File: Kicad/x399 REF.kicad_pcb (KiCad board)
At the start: 2 copper layers, 106 x 56 mm, 57 parts, among them J1 +15V, J2 10Vref, Q1 MMBT3904, Q2 2SD882, U1 LM399, U2 OP07

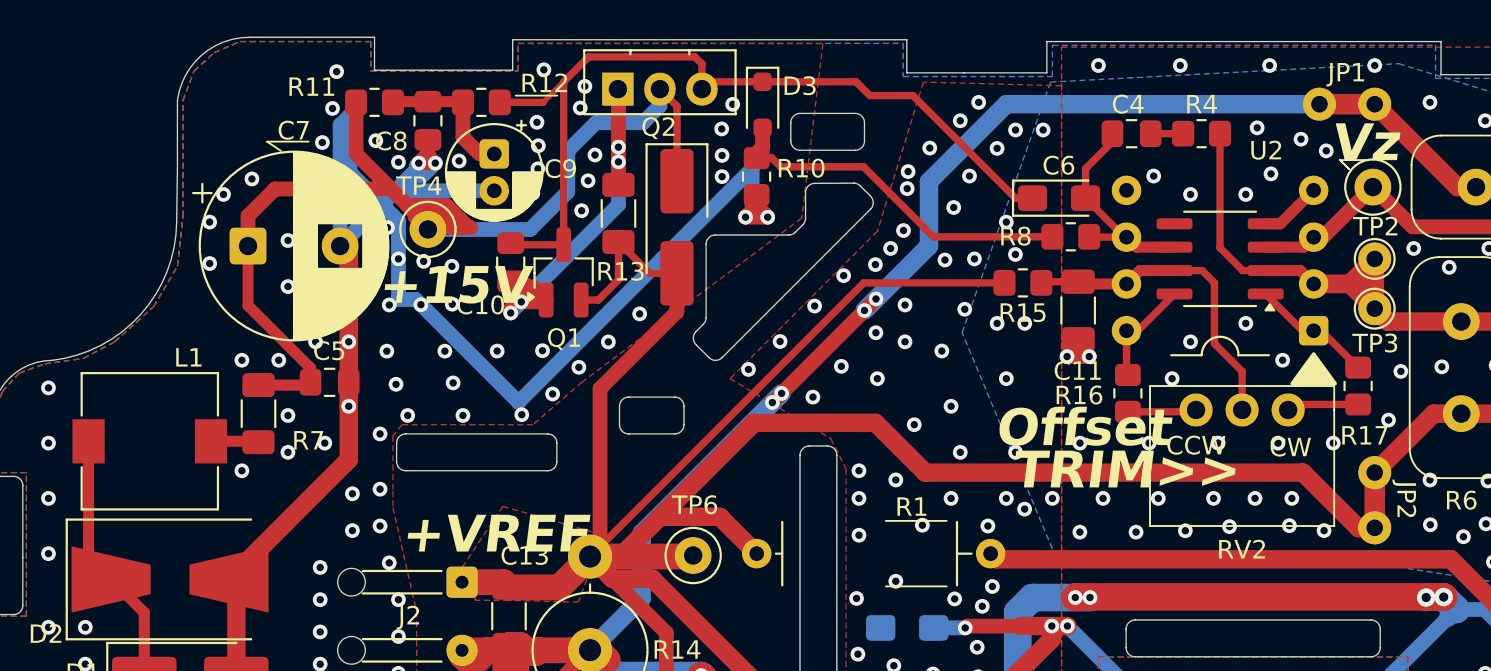
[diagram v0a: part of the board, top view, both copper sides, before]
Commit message: Replace DIP8-400mil wide footprint to standard 300mil
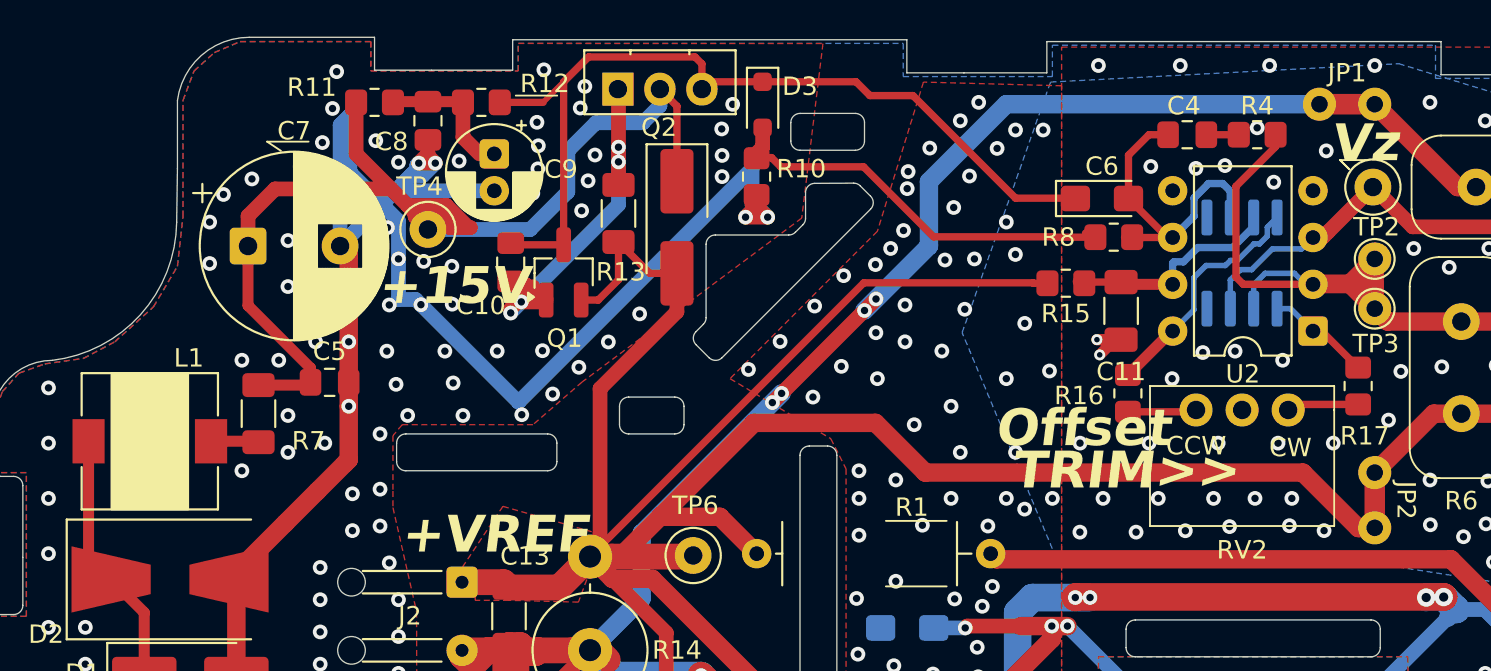
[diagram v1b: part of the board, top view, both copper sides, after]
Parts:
- U2: footprint Package_DIP:DIP-8_W7.62mm_PLUS SOIC -> Package_DIP:DIP-8_W7.62mm_W_soic_under
- moved C4 3.02 mm to (108.5, 72.6)
- moved R4 3.02 mm to (112.2, 72.6)
- moved C11 2.33 mm to (104.9, 82.2)
- moved C6 2.33 mm to (103.8, 76.1)
- moved R15 2.33 mm to (101.9, 80.7)
- moved R8 2.33 mm to (104.5, 78.2)
- moved U2 1.23 mm to (115.3, 83.3)
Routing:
- net Net-(U2A--): track 53.7 -> 61.6 mm
- net Net-(R16-Pad1): track 5.86 -> 12.9 mm
- net Net-(U2B-V+): track 17.6 -> 11.7 mm
- net Net-(U2A-+): track 151.3 -> 156.4 mm
- net Earth: track 172.2 -> 167.4 mm, vias 342 -> 341
- net Net-(C4-Pad2): track 12.4 -> 16.9 mm
- net Net-(D3-A): track 19.9 -> 22.6 mm
- net +10VREF: track 203.8 -> 206.2 mm
- net Net-(D3-K): track 48.0 -> 50.3 mm

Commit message: Add files via upload
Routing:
- net Net-(U2B-V+): track 11.7 -> 19.7 mm
- net Net-(C4-Pad2): track 16.9 -> 14.6 mm
- net Net-(U2A--): track 61.6 -> 61.0 mm
- net Earth: vias 341 -> 342
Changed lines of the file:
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@@
 	)
 	(via
-		(at 127.631352 96.867477)
+		(at 127.95 97.825)
 		(size 0.8)
 		(drill 0.4)
@@
 	)
 	(via
-		(at 111.05 84.375)
+		(at 115.95 85.4)
 		(size 0.8)
 		(drill 0.4)
@@
 	)
 	(via
-		(at 113.631352 84.867477)
+		(at 114 85.4)
 		(size 0.8)
 		(drill 0.4)
@@
 	)
 	(via
-		(at 125.075 95.825)
+		(at 125.55 96.25)
 		(size 0.8)
 		(drill 0.4)
@@
 	)
 	(via
+		(at 112.85 84.3)
+		(size 0.8)
+		(drill 0.4)
+		(layers "F.Cu" "B.Cu")
+		(free yes)
+		(net 2)
+	)
+	(via
 		(at 99.125 79.125)
 		(size 0.8)
@@
 	)
 	(segment
-		(start 112.0618 80.7632)
-		(end 112.0618 82.067202)
-		(width 0.3)
-		(layer "B.Cu")
-		(net 4)
-	)
-	(segment
-		(start 115.28 80.745)
-		(end 114.87 80.745)
-		(width 0.3)
+		(start 112.0618 82.067202)
+		(end 112.0618 81.0632)
+		(width 0.4)
 		(layer "B.Cu")
 		(net 4)
 	)
 	(segment
-		(start 112.675 80.15)
-		(end 112.0618 80.7632)
-		(width 0.3)
+		(start 115.21 80.675)
+		(end 115.28 80.745)
+		(width 0.4)
 		(layer "B.Cu")
 		(net 4)
 	)
 	(segment
-		(start 114.275 80.15)
-		(end 112.675 80.15)
-		(width 0.3)
+		(start 112.45 80.675)
+		(end 115.21 80.675)
+		(width 0.4)
 		(layer "B.Cu")
 		(net 4)
 	)
 	(segment
-		(start 114.87 80.745)
-		(end 114.275 80.15)
-		(width 0.3)
+		(start 112.0618 81.0632)
+		(end 112.45 80.675)
+		(width 0.4)
 		(layer "B.Cu")
 		(net 4)
@@
 	)
 	(segment
-		(start 110.791799 75.691799)
-		(end 110.791799 77.117201)
-		(width 0.4)
-		(layer "B.Cu")
-		(net 5)
-	)
-	(segment
-		(start 110.375 75.275)
-		(end 110.791799 75.691799)
+		(start 110.025 78.575)
+		(end 108.03 78.575)
 		(width 0.4)
 		(layer "B.Cu")
@@
 	)
 	(segment
-		(start 108.8208 76.059813)
-		(end 109.605613 75.275)
+		(start 110.791799 77.117201)
+		(end 110.791799 77.808201)
 		(width 0.4)
 		(layer "B.Cu")
@@
 	)
 	(segment
-		(start 107.66 78.205)
-		(end 108.8208 77.0442)
+		(start 108.03 78.575)
+		(end 107.66 78.205)
 		(width 0.4)
 		(layer "B.Cu")
@@
 	)
 	(segment
-		(start 109.605613 75.275)
-		(end 110.375 75.275)
-		(width 0.4)
-		(layer "B.Cu")
-		(net 5)
-	)
-	(segment
-		(start 108.8208 77.0442)
-		(end 108.8208 76.059813)
+		(start 110.791799 77.808201)
+		(end 110.025 78.575)
 		(width 0.4)
 		(layer "B.Cu")
@@
 	)
 	(segment
+		(start 111.431352 87.567477)
+		(end 111.431352 84.456352)
+		(width 0.4)
+		(layer "F.Cu")
+		(net 11)
+	)
+	(segment
 		(start 102.651352 80.724977)
 		(end 102.531352 80.604977)
@@
 	)
 	(segment
-		(start 107.66 80.745)
-		(end 104.9825 80.745)
-		(width 0.6)
+		(start 111.431352 84.456352)
+		(end 107.72 80.745)
+		(width 0.4)
 		(layer "F.Cu")
 		(net 11)
 	)
 	(segment
-		(start 110.917388 78.75)
-		(end 109.025 78.75)
+		(start 107.72 80.745)
+		(end 107.66 80.745)
 		(width 0.4)
-		(layer "B.Cu")
+		(layer "F.Cu")
 		(net 11)
 	)
 	(segment
-		(start 112.0618 77.117201)
-		(end 112.0618 77.605588)
-		(width 0.4)
-		(layer "B.Cu")
+		(start 107.66 80.745)
+		(end 104.9825 80.745)
+		(width 0.6)
+		(layer "F.Cu")
 		(net 11)
 	)
 	(segment
-		(start 107.725 79.525)
-		(end 107.66 79.59)
+		(start 112.0618 77.117201)
+		(end 112.0618 77.9132)
 		(width 0.4)
 		(layer "B.Cu")
@@
 	)
 	(segment
-		(start 107.66 79.59)
-		(end 107.66 80.745)
+		(start 108.9 79.375)
+		(end 107.66 80.615)
 		(width 0.4)
 		(layer "B.Cu")
@@
 	)
 	(segment
-		(start 109.025 78.75)
-		(end 108.25 79.525)
+		(start 110.6 79.375)
+		(end 108.9 79.375)
 		(width 0.4)
 		(layer "B.Cu")
@@
 	)
 	(segment
-		(start 108.25 79.525)
-		(end 107.725 79.525)
+		(start 112.0618 77.9132)
+		(end 110.6 79.375)
 		(width 0.4)
 		(layer "B.Cu")
@@
 	)
 	(segment
-		(start 112.0618 77.605588)
-		(end 110.917388 78.75)
+		(start 107.66 80.615)
+		(end 107.66 80.745)
 		(width 0.4)
 		(layer "B.Cu")
@@
 	)
 	(segment
+		(start 97.781352 95.367477)
+		(end 98.188875 95.775)
+		(width 1)
+		(layer "F.Cu")
+		(net 17)
+	)
+	(segment
+		(start 122.875 95.775)
+		(end 127.775 100.675)
+		(width 1)
+		(layer "F.Cu")
+		(net 17)
+	)
+	(segment
 		(start 133.6 85.2)
 		(end 133.6 84.375)
@@
 	)
 	(segment
+		(start 127.775 100.675)
+		(end 130.85 100.675)
+		(width 1)
+		(layer "F.Cu")
+		(net 17)
+	)
+	(segment
 		(start 120.688875 77.625)
 		(end 118.531352 75.467477)
@@
 	)
 	(segment
-		(start 98.088875 95.675)
-		(end 122.775 95.675)
+		(start 98.188875 95.775)
+		(end 122.875 95.775)
 		(width 1)
 		(layer "F.Cu")
@@
 	)
 	(segment
-		(start 97.781352 95.367477)
-		(end 98.088875 95.675)
-		(width 1)
-		(layer "F.Cu")
-		(net 17)
-	)
-	(segment
 		(start 127.225 78.95)
 		(end 125.9 77.625)
@@
 	)
 	(segment
-		(start 127.775 100.675)
-		(end 130.85 100.675)
-		(width 1)
-		(layer "F.Cu")
-		(net 17)
-	)
-	(segment
 		(start 125.9 77.625)
 		(end 120.688875 77.625)
@@
 	)
 	(segment
-		(start 122.775 95.675)
-		(end 127.775 100.675)
-		(width 1)
-		(layer "F.Cu")
-		(net 17)
-	)
-	(segment
 		(start 116.111914 77.886914)
 		(end 118.531352 75.467477)
@@
 	)
 	(segment
-		(start 111.35 79.95)
-		(end 110.7918 80.5082)
-		(width 0.3)
+		(start 113.7 79.825)
+		(end 113.7 79.785)
+		(width 0.4)
 		(layer "B.Cu")
 		(net 17)
@@
 	)
 	(segment
-		(start 114.66 78.825)
-		(end 113.075 78.825)
-		(width 0.3)
+		(start 112.325 79.825)
+		(end 113.7 79.825)
+		(width 0.4)
 		(layer "B.Cu")
 		(net 17)
@@
 	)
 	(segment
-		(start 110.7918 80.5082)
-		(end 110.7918 82.067201)
-		(width 0.3)
+		(start 110.7918 82.067201)
+		(end 110.7918 81.3582)
+		(width 0.4)
 		(layer "B.Cu")
 		(net 17)
@@
 	)
 	(segment
-		(start 113.075 78.825)
-		(end 111.95 79.95)
-		(width 0.3)
+		(start 113.7 79.785)
+		(end 115.28 78.205)
+		(width 0.4)
 		(layer "B.Cu")
 		(net 17)
@@
 	)
 	(segment
-		(start 115.28 78.205)
-		(end 114.66 78.825)
-		(width 0.3)
-		(layer "B.Cu")
-		(net 17)
-	)
-	(segment
 		(start 128.425 78.95)
 		(end 127.625 78.95)
@@
 	)
 	(segment
+		(start 110.7918 81.3582)
+		(end 112.325 79.825)
+		(width 0.4)
+		(layer "B.Cu")
+		(net 17)
+	)
+	(segment
 		(start 131.85 100.675)
 		(end 131.85 101.325)
@@
 	)
 	(segment
-		(start 111.95 79.95)
-		(end 111.35 79.95)
-		(width 0.3)
-		(layer "B.Cu")
-		(net 17)
-	)
-	(segment
 		(start 133.575 102.1)
 		(end 133.575 109.6)
@@
 	)
 	(segment
-		(start 111.176 79.449)
-		(end 112.075 78.55)
-		(width 0.3)
-		(layer "B.Cu")
-		(net 19)
-	)
-	(segment
-		(start 112.8 77.649002)
-		(end 113.331801 77.117201)
-		(width 0.3)
-		(layer "B.Cu")
-		(net 19)
-	)
-	(segment
-		(start 108.811 82.134)
-		(end 108.811 80.389)
-		(width 0.3)
-		(layer "B.Cu")
-		(net 19)
-	)
-	(segment
-		(start 112.375 78.55)
-		(end 112.8 78.125)
-		(width 0.3)
+		(start 113.331801 77.843199)
+		(end 110.875 80.3)
+		(width 0.4)
 		(layer "B.Cu")
 		(net 19)
 	)
 	(segment
-		(start 110.801 79.449)
-		(end 111.176 79.449)
+		(start 109.4 80.55)
+		(end 109.351323 80.55)
 		(width 0.3)
 		(layer "B.Cu")
@@
 	)
 	(segment
-		(start 107.66 83.285)
-		(end 108.811 82.134)
+		(start 108.775 81.126323)
+		(end 108.775 82.17)
 		(width 0.3)
 		(layer "B.Cu")
@@
 	)
 	(segment
-		(start 110.525 79.725)
-		(end 110.801 79.449)
-		(width 0.3)
+		(start 113.331801 77.117201)
+		(end 113.331801 77.843199)
+		(width 0.4)
 		(layer "B.Cu")
 		(net 19)
 	)
 	(segment
-		(start 112.075 78.55)
-		(end 112.375 78.55)
-		(width 0.3)
+		(start 110.875 80.3)
+		(end 109.65 80.3)
+		(width 0.4)
 		(layer "B.Cu")
 		(net 19)
 	)
 	(segment
-		(start 108.811 80.389)
-		(end 109.475 79.725)
+		(start 109.351323 80.55)
+		(end 108.775 81.126323)
 		(width 0.3)
 		(layer "B.Cu")
@@
 	)
 	(segment
-		(start 112.8 78.125)
-		(end 112.8 77.649002)
-		(width 0.3)
+		(start 109.65 80.3)
+		(end 109.4 80.55)
+		(width 0.4)
 		(layer "B.Cu")
 		(net 19)
 	)
 	(segment
-		(start 109.475 79.725)
-		(end 110.525 79.725)
+		(start 108.775 82.17)
+		(end 107.66 83.285)
 		(width 0.3)
 		(layer "B.Cu")

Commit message: Add files via upload
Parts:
- removed D1: SS34A, Diode_SMD:D_SMA_Handsoldering
- added C14: 100n, Capacitor_SMD:C_0805_2012Metric_Pad1.18x1.45mm_HandSolder, B.Cu at (85.8, 106.8)
- added C15: 100n, Capacitor_SMD:C_0805_2012Metric_Pad1.18x1.45mm_HandSolder, B.Cu at (85.7, 103.0)
- added C16: 1u, Capacitor_SMD:C_1206_3216Metric_Pad1.33x1.80mm_HandSolder, B.Cu at (83.5, 108.8)
- added C17: 1u, Capacitor_SMD:C_1206_3216Metric_Pad1.33x1.80mm_HandSolder, B.Cu at (89.2, 111.0)
- added C18: 1u, Capacitor_SMD:C_1206_3216Metric_Pad1.33x1.80mm_HandSolder, B.Cu at (83.5, 100.0)
- added C19: 1u, Capacitor_SMD:C_1206_3216Metric_Pad1.33x1.80mm_HandSolder, B.Cu at (89.2, 98.6)
- added D6: BZX384B12, Diode_SMD:D_SOD-323_HandSoldering, F.Cu at (71.8, 49.9)
- added F2: 0ZCG0075BF2B, Resistor_SMD:R_1812_4532Metric_Pad1.30x3.40mm_HandSolder, F.Cu at (58.7, 70.7)
- added FL1: DR331-474BE, OwnStuff:L_CommonMode_Bourns_DR331_Handsolder, F.Cu at (52.5, 81.6)
- added FL2: 28mH, OwnStuff:Universal line filter, F.Cu at (89.7, 104.9)
- added J3: Guard, Connector_Wire:SolderWire-0.127sqmm_1x01_D0.48mm_OD1mm_Relief, F.Cu at (60.6, 43.5)
- added JP3: ~, TestPoint:TestPoint_2Pads_Pitch2.54mm_Drill0.8mm, F.Cu at (44.6, 71.3)
- added JP4: ~, TestPoint:TestPoint_2Pads_Pitch2.54mm_Drill0.8mm, F.Cu at (51.3, 82.8)
- added JP5: ~, TestPoint:TestPoint_2Pads_Pitch2.54mm_Drill0.8mm, F.Cu at (51.3, 80.3)
- added Q3: AON7410, OwnStuff:AO DFN3x3 EP GDS, F.Cu at (61.0, 76.0)
- added R18: 470R, Resistor_SMD:R_0805_2012Metric_Pad1.20x1.40mm_HandSolder, B.Cu at (81.4, 106.3)
- added R19: 470R, Resistor_SMD:R_0805_2012Metric_Pad1.20x1.40mm_HandSolder, B.Cu at (89.0, 106.7)
- added R20: 470R, Resistor_SMD:R_0805_2012Metric_Pad1.20x1.40mm_HandSolder, B.Cu at (83.5, 104.4)
- added R21: 470R, Resistor_SMD:R_0805_2012Metric_Pad1.20x1.40mm_HandSolder, B.Cu at (89.0, 102.9)
- added R22: 1k, Resistor_SMD:R_0805_2012Metric_Pad1.20x1.40mm_HandSolder, F.Cu at (71.8, 53.8)
- added R23: smd, Resistor_SMD:R_1206_3216Metric_Pad1.30x1.75mm_HandSolder, F.Cu at (122.3, 92.0)
- JP1, JP2: footprint Jumper:Joined holes D=1.8 Dh=0.9 P=3mm -> OwnStuff:Joined holes D=1.8 Dh=0.9 P=3mm
- L1: footprint Inductor_SMD:L_7.3x7.3_H4.5_Handsoldering -> OwnStuff:L_7.3x7.3_H4.5_Handsoldering
- R13, R7: value 6R2 -> 6R8
- R3, R5, R6: footprint Resistor_THT:S5-61 -> OwnStuff:S5-61+vishay(150mil)+smd1206
- RV1, RV2: footprint Potentiometer_THT:Potentiometer_Soviet_SP5-2VB -> OwnStuff:Potentiometer_Soviet_SP5-2VB
- TP2, TP3: footprint TestPoint:TestPoint_THTPad_D1.8mm_Drill0.9mm -> OwnStuff:TestPoint_THTPad_D1.8mm_Drill0.9mm
- U1: footprint Package_TO_SOT_THT:Analog_TO-46-4_ThermalShield_balanced pins -> OwnStuff:Analog_TO-46-4_ThermalShield_balanced pins
- U2: footprint Package_DIP:DIP-8_W7.62mm_W_soic_under -> OwnStuff:DIP-8_W7.62mm_W_soic_under
- moved J1 43.6 mm to (97.2, 110.4), turned to 0 degrees
- moved F1 41.8 mm to (97.5, 108.1), turned to 180 degrees
- moved R9 29.6 mm to (168.4, 83.4)
- moved TP6 29.4 mm to (109.5, 86.2)
- moved C11 29.3 mm to (134.0, 78.8)
- moved R15 29.3 mm to (131.0, 77.3)
- moved R6 29.3 mm to (152.4, 81.9)
- moved U1 29.3 mm to (142.6, 107.5)
- moved C1 29.3 mm to (122.3, 96.0)
- moved C10 29.3 mm to (100.8, 76.2)
- moved C12 29.3 mm to (107.8, 101.9)
- moved C2 29.3 mm to (160.6, 102.1)
- moved C8 29.3 mm to (96.3, 68.5)
- moved C9 29.3 mm to (99.9, 70.3)
- moved D4 29.3 mm to (109.8, 74.3)
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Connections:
- C3 pad 1: Net-(D1-K) -> Net-(C14-Pad2)
- C5 pad 1: Net-(D4-K) -> Net-(D2-K)
- C7 pad 1: Net-(D4-K) -> Net-(D2-K)
- D2 pad 1: Net-(D1-K) -> Net-(D2-K)
- D4 pad 1: Net-(D4-K) -> Net-(D2-K)
- F1 pad 2: Net-(D1-K) -> Net-(F1-Pad2)
- J1 pad 2: Earth -> Net-(J1-Pin_2)
- J2 pad 1: +10VREF -> Net-(J2-Pin_1)
- J2 pad 2: MGND -> Net-(J2-Pin_2)
- L1 pad 1: Net-(D1-K) -> Net-(C14-Pad2)
- Q2 pad 2: Net-(D4-K) -> Net-(D2-K)
- R11 pad 2: Net-(D4-K) -> Net-(D2-K)
- R7 pad 2: Net-(D4-K) -> Net-(D2-K)
- TP4 pad 1: Net-(D4-K) -> Net-(D2-K)
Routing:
- net Earth: track 167.4 -> 49.4 mm, vias 342 -> 221
- net +10VREF: track 206.2 -> 115.2 mm, vias 3 -> 4
- net MGND: track 282.2 -> 196.0 mm, vias 13 -> 11
- net Net-(D4-K): track 60.4 -> 0.00 mm
- net Net-(D2-K): track 0.00 -> 31.0 mm
- net Net-(D1-K): track 23.8 -> 0.00 mm
- net Net-(C14-Pad2): track 0.00 -> 23.1 mm
- net Net-(J1-Pin_2): track 0.00 -> 17.0 mm
- net Guard: track 0.00 -> 11.3 mm
- net Net-(R9-Pad2): track 71.2 -> 62.9 mm
- net Net-(U2A-+): track 155.9 -> 163.1 mm
- net Net-(F1-Pad2): track 0.00 -> 6.23 mm
- net Net-(L1-Pad2): track 2.60 -> 4.92 mm
- net Net-(C17-Pad1): track 0.00 -> 2.14 mm
- net Net-(C16-Pad1): track 0.00 -> 2.13 mm
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- removed copper zone on F.Cu, net +10VREF
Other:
- outline, holes or cut-outs redrawn

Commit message: Add files via upload
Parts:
- added C20: 100n, Capacitor_SMD:C_0805_2012Metric_Pad1.18x1.45mm_HandSolder, B.Cu at (88.0, 108.7)
- added C21: 100n, Capacitor_SMD:C_0805_2012Metric_Pad1.18x1.45mm_HandSolder, B.Cu at (85.9, 108.8)
- added C22: 1u, Capacitor_THT:C_Rect_L4.6mm_W5.5mm_P2.50mm_MKS02_FKP02, F.Cu at (89.9, 111.9)
- added C23: 1u, Capacitor_THT:C_Rect_L4.6mm_W5.5mm_P2.50mm_MKS02_FKP02, F.Cu at (83.9, 109.1)
- added H4: d=3.7, OwnStuff:MountingHole_3.7mm_Pad_Via_6.7mm diameter, F.Cu at (84.9, 116.5)
- added R23: 47R, Resistor_SMD:R_0805_2012Metric_Pad1.20x1.40mm_HandSolder, B.Cu at (91.5, 109.0)
- added R24: 47R, Resistor_SMD:R_0805_2012Metric_Pad1.20x1.40mm_HandSolder, B.Cu at (83.9, 106.8)
- C11: renamed from C5; moved to B.Cu
- C4: renamed from C16; footprint Capacitor_SMD:C_1206_3216Metric_Pad1.33x1.80mm_HandSolder -> Capacitor_SMD:C_0805_2012Metric_Pad1.18x1.45mm_HandSolder
- C5: renamed from C18; footprint Capacitor_SMD:C_1206_3216Metric_Pad1.33x1.80mm_HandSolder -> Capacitor_SMD:C_0805_2012Metric_Pad1.18x1.45mm_HandSolder
- C6: renamed from C17; footprint Capacitor_SMD:C_1206_3216Metric_Pad1.33x1.80mm_HandSolder -> Capacitor_SMD:C_0805_2012Metric_Pad1.18x1.45mm_HandSolder
- C7: renamed from C19; footprint Capacitor_SMD:C_1206_3216Metric_Pad1.33x1.80mm_HandSolder -> Capacitor_SMD:C_0805_2012Metric_Pad1.18x1.45mm_HandSolder
- D1: renamed from D2; moved to B.Cu
- H3: renamed from H1; footprint MountingHole:MountingHole_3.7mm_Pad_Via -> OwnStuff:MountingHole_3.7mm_Pad_Via_6.7mm diameter
- NT1: moved to B.Cu
- Q3: footprint OwnStuff:AO DFN3x3 EP GDS -> OwnStuff:AO DFN3x3 EP GDS Handsoldering
- R8: renamed from R7; moved to B.Cu
- moved J2 77.8 mm to (99.8, 110.7), turned to 90 degrees
- moved JP5 66.3 mm to (102.8, 103.1), turned to -90 degrees
- moved H3 53.5 mm to (85.0, 68.4)
- moved D4 51.8 mm to (79.0, 101.2), turned to 90 degrees
- moved JP3 48.1 mm to (91.8, 106.3)
- moved FL2 46.7 mm to (93.0, 105.0)
- moved JP4 45.5 mm to (91.8, 103.7)
- moved R19 45.0 mm to (82.3, 97.5), turned to 180 degrees
- moved F2 42.9 mm to (83.9, 105.4), turned to 0 degrees
- moved C6 37.3 mm to (86.1, 73.8), turned to 0 degrees
- moved F1 35.3 mm to (73.4, 82.4), turned to 90 degrees
- moved R3 33.5 mm to (82.3, 73.9), turned to 180 degrees
- moved Q3 33.0 mm to (82.3, 101.2), turned to 180 degrees
- moved C4 32.3 mm to (87.1, 76.7), turned to 90 degrees
- moved J1 30.9 mm to (74.5, 89.3)
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- renumbered C14 to C1, C4 to C10, C6 to C12, C7 to C13, C8 to C14, C9 to C15, C10 to C16, C12 to C17, C13 to C18, C11 to C19, C15 to C2, C1 to C3, C3 to C8, C2 to C9, D3 to D2, D4 to D3, D6 to D4, FL2 to FL1, FL1 to FL2, H2 to H1, H3 to H2, J3 to J2, J2 to J3, JP5 to JP3, JP3 to JP5, R18 to R1, R5 to R10, R6 to R11, R8 to R12, R9 to R13, R10 to R14, R11 to R15, R12 to R16, R13 to R17, R14 to R18, R22 to R19, R23 to R1alt1, R20 to R2, R15 to R20, R16 to R21, R17 to R22, R19 to R3, R21 to R4, R1 to R5, R2 to R6, R3 to R7, R4 to R9, TP6 to TP5, TP5 to TP6
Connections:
- C1 pad 1: Guard -> Guard1
- C2 pad 2: Guard -> Guard1
- F2 pad 2: Net-(JP5-A) -> Net-(JP3-A)
- FL2 pad 1: Net-(JP5-A) -> MGND
- FL2 pad 2: MGND -> Net-(JP3-A)
- FL2 pad 3: Net-(J2-Pin_2) -> Net-(J3-Pin_1)
- FL2 pad 4: Net-(J2-Pin_1) -> Net-(J3-Pin_2)
- H3 pad 1: Earth -> Guard1
- J2 pad 1: Guard -> Guard2
- J3 pad 1: Net-(J2-Pin_1) -> Net-(J3-Pin_1)
- J3 pad 2: Net-(J2-Pin_2) -> Net-(J3-Pin_2)
- JP3 pad 1: Net-(JP5-A) -> Net-(JP3-A)
- JP3 pad 2: Net-(J2-Pin_1) -> Net-(J3-Pin_1)
- JP4 pad 2: Net-(J2-Pin_2) -> Net-(J3-Pin_2)
- JP5 pad 1: Net-(J2-Pin_2) -> Net-(J3-Pin_2)
- JP5 pad 2: Guard -> Guard2
- R1 pad 2: Guard -> Guard1
- R2 pad 1: Guard -> Guard1
- R3 pad 2: Guard -> Guard1
- R4 pad 1: Guard -> Guard1
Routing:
- net +10VREF: track 115.2 -> 300.7 mm, vias 4 -> 6
- net MGND: track 196.0 -> 343.1 mm, vias 11 -> 15
- net Guard2: track 0.00 -> 110.7 mm, vias 0 -> 2
- net Guard1: track 0.00 -> 38.4 mm
- net Earth: track 49.4 -> 83.8 mm, vias 221 -> 212
- net Net-(D1-K): track 31.0 -> 51.0 mm
- net Net-(JP3-A): track 0.00 -> 16.1 mm, vias 0 -> 2
- net Net-(J1-Pin_2): track 17.0 -> 5.54 mm
- net Guard: track 11.3 -> 0.00 mm
- net Net-(J3-Pin_2): track 0.00 -> 8.54 mm
- net Net-(J3-Pin_1): track 0.00 -> 6.03 mm
- net Net-(D4-A): track 0.00 -> 5.36 mm
- net Net-(F1-Pad2): track 6.23 -> 9.99 mm
- net Net-(J1-Pin_1): track 2.79 -> 6.47 mm
- net Net-(C1-Pad2): track 23.1 -> 26.3 mm
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- added copper zone on F.Cu, net +10VREF
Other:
- outline, holes or cut-outs redrawn
- board text added: "+"
- board text added: "+10V"
- board text added: "-"
- board text added: "0V"
- board text added: "D3"
- board text added: "Guard"
- board text added: "VREF"
- board text added: "Vref OUT"
- board text removed: "+VREF"
- board text removed: "MGND"
